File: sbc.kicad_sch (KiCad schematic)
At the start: 2 parts, among them J5 Raspberry_Pi_2_3, J6 Conn_02x07_Odd_Even

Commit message: improve design
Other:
- title: (none) -> Dropbot
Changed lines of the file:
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@@
 	(generator_version "10.0")
 	(paper "A4")
+	(title_block
+		(title "Dropbot")
+	)
 	(junction
 		(at 170.18 92.71)

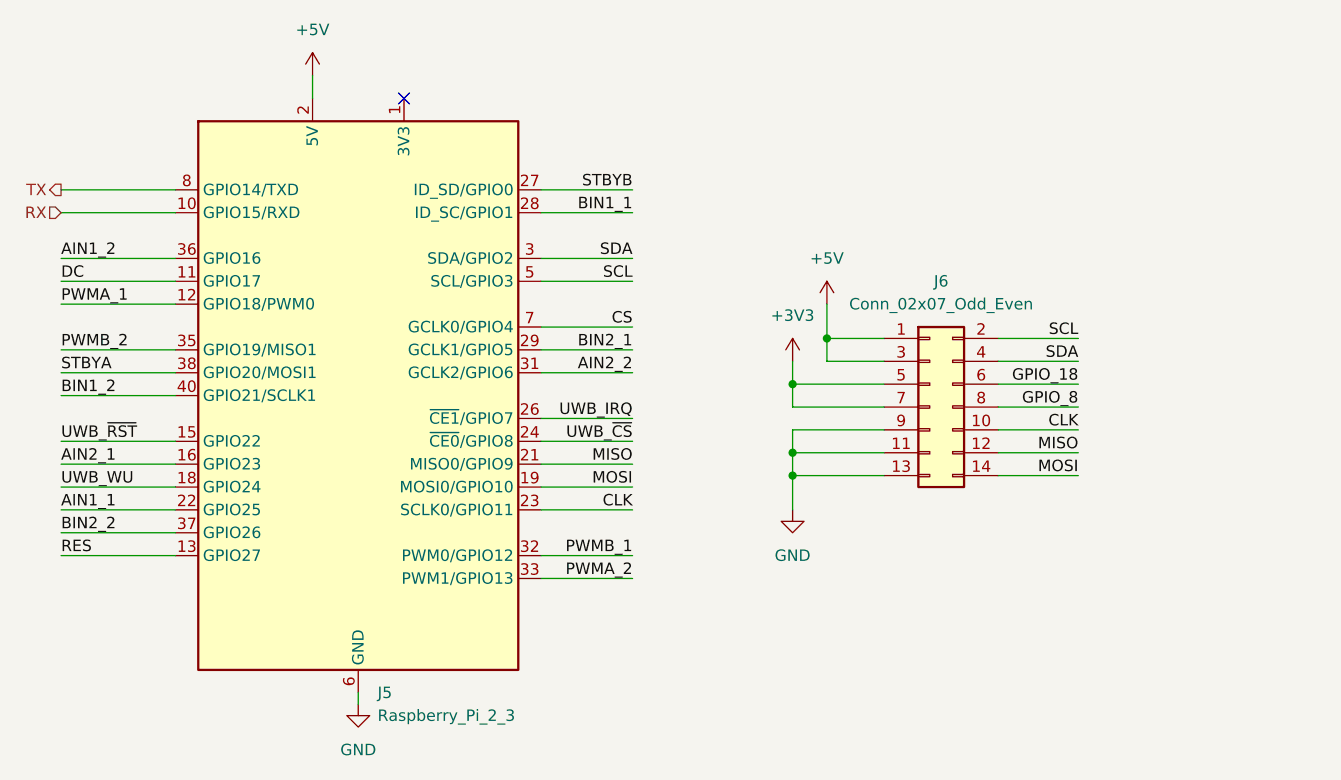
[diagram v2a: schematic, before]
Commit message: consolidated routing
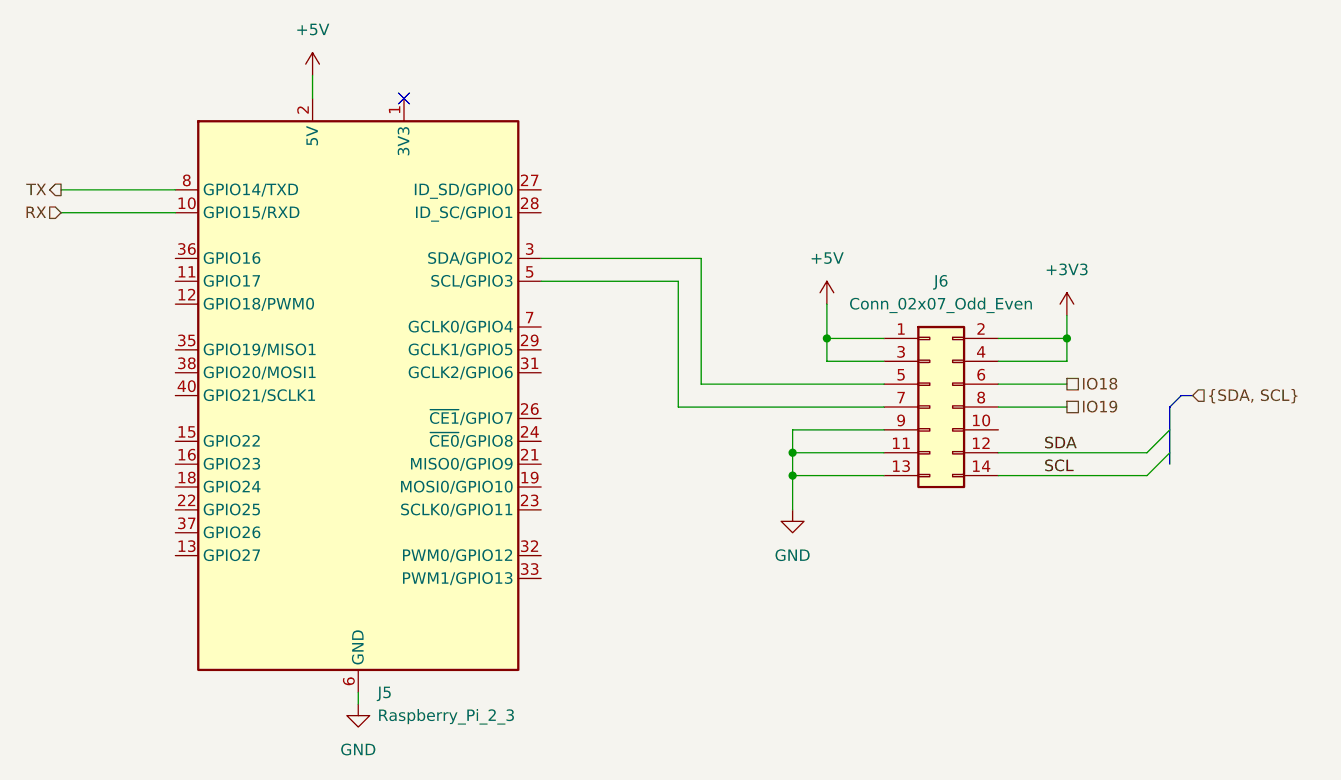
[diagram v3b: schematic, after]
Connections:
- net +3V3: now also J6.2 (Pin_2), J6.4 (Pin_4); no longer J6.5 (Pin_5), J6.7 (Pin_7)
- net SCL: now also J6.14 (Pin_14); no longer J5.5 (SCL/GPIO3), J6.2 (Pin_2)
- net SDA: now also J6.12 (Pin_12); no longer J5.3 (SDA/GPIO2), J6.4 (Pin_4)
- net AIN1_1: no longer names the net of J5.22 (GPIO25)
- net AIN1_2: no longer names the net of J5.36 (GPIO16)
- net AIN2_1: no longer names the net of J5.16 (GPIO23)
- net AIN2_2: no longer names the net of J5.31 (GCLK2/GPIO6)
- net BIN1_1: no longer names the net of J5.28 (ID_SC/GPIO1)
- net BIN1_2: no longer names the net of J5.40 (GPIO21/SCLK1)
- net BIN2_1: no longer names the net of J5.29 (GCLK1/GPIO5)
- net BIN2_2: no longer names the net of J5.37 (GPIO26)
- net CLK: no longer names the net of J6.10 (Pin_10)
- net CLK: no longer J5.23 (SCLK0/GPIO11)
- net CS: no longer names the net of J5.7 (GCLK0/GPIO4)
- net DC: no longer names the net of J5.11 (GPIO17)
- net GPIO_18 renamed IO18
- net GPIO_8 renamed IO19
- net MISO: no longer names the net of J5.21 (MISO0/GPIO9)
- net MISO: no longer J6.12 (Pin_12)
- net MOSI: no longer names the net of J5.19 (MOSI0/GPIO10)
- net MOSI: no longer J6.14 (Pin_14)
- net PWMA_1: no longer names the net of J5.12 (GPIO18/PWM0)
- net PWMA_2: no longer names the net of J5.33 (PWM1/GPIO13)
- net PWMB_1: no longer names the net of J5.32 (PWM0/GPIO12)
- net PWMB_2: no longer names the net of J5.35 (GPIO19/MISO1)
- net RES: no longer names the net of J5.13 (GPIO27)
- net STBYA: no longer names the net of J5.38 (GPIO20/MOSI1)
- net STBYB: no longer names the net of J5.27 (ID_SD/GPIO0)
- net UWB_IRQ: no longer names the net of J5.26 (~{CE1}/GPIO7)
- net UWB_WU: no longer names the net of J5.18 (GPIO24)
- net UWB_~{CS}: no longer names the net of J5.24 (~{CE0}/GPIO8)
- net UWB_~{RST}: no longer names the net of J5.15 (GPIO22)
- new net: J5.3 (SDA/GPIO2), J6.5 (Pin_5)
- new net: J5.5 (SCL/GPIO3), J6.7 (Pin_7)

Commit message: complete routing and validated ERC/DRC
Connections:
- no-connect marks 1 -> 26
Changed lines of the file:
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@@
+	)
+	(no_connect
+		(at 101.6 93.98)
+	)
+	(no_connect
+		(at 142.24 111.76)
 	)
 	(no_connect
 		(at 127 60.96)
 	)
+	(no_connect
+		(at 101.6 101.6)
+	)
+	(no_connect
+		(at 142.24 104.14)
+	)
+	(no_connect
+		(at 101.6 111.76)
+	)
+	(no_connect
+		(at 142.24 114.3)
+	)
+	(no_connect
+		(at 142.24 96.52)
+	)
+	(no_connect
+		(at 101.6 83.82)
+	)
+	(no_connect
+		(at 101.6 78.74)
+	)
+	(no_connect
+		(at 142.24 101.6)
+	)
+	(no_connect
+		(at 101.6 88.9)
+	)
+	(no_connect
+		(at 142.24 99.06)
+	)
+	(no_connect
+		(at 101.6 99.06)
+	)
+	(no_connect
+		(at 193.04 97.79)
+	)
+	(no_connect
+		(at 142.24 91.44)
+	)
+	(no_connect
+		(at 142.24 88.9)
+	)
+	(no_connect
+		(at 142.24 71.12)
+	)
+	(no_connect
+		(at 142.24 86.36)
+	)
+	(no_connect
+		(at 142.24 106.68)
+	)
+	(no_connect
+		(at 101.6 109.22)
+	)
+	(no_connect
+		(at 101.6 81.28)
+	)
+	(no_connect
+		(at 101.6 106.68)
+	)
+	(no_connect
+		(at 142.24 73.66)
+	)
+	(no_connect
+		(at 101.6 104.14)
+	)
+	(no_connect
+		(at 101.6 91.44)
+	)
 	(bus_entry

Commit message: tentative automatic population
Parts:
- J5: LCSC (none) -> C22436166; MPN (none) -> HC-PM254-8.5H-2x20PS; Manufacturer (none) -> Hong Cheng
- J6: LCSC (none) -> C492424; MPN (none) -> PZ254V-12-14P; Manufacturer (none) -> XFCN
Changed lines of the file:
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@@
 			)
 		)
-		(property "Datasheet" ""
+		(property "Datasheet" "https://datasheet.lcsc.com/datasheet/pdf/7e4d55c01d5aeb1046c811fdaf9e5359.pdf?productCode=C492424"
 			(at 185.42 95.25 0)
 			(hide yes)
@@
 					(size 1.27 1.27)
 				)
+			)
+		)
+		(property "Manufacturer" "XFCN" (at 0 0 0)
+			(effects
+				(font
+					(size 1.27 1.27)
+				)
+				(hide yes)
+			)
+		)
+		(property "MPN" "PZ254V-12-14P" (at 0 0 0)
+			(effects
+				(font
+					(size 1.27 1.27)
+				)
+				(hide yes)
+			)
+		)
+		(property "LCSC" "C492424" (at 0 0 0)
+			(effects
+				(font
+					(size 1.27 1.27)
+				)
+				(hide yes)
 			)
 		)
@@
 			)
 		)
+		(property "Manufacturer" "Hong Cheng" (at 0 0 0)
+			(effects
+				(font
+					(size 1.27 1.27)
+				)
+				(hide yes)
+			)
+		)
+		(property "MPN" "HC-PM254-8.5H-2x20PS" (at 0 0 0)
+			(effects
+				(font
+					(size 1.27 1.27)
+				)
+				(hide yes)
+			)
+		)
+		(property "LCSC" "C22436166" (at 0 0 0)
+			(effects
+				(font
+					(size 1.27 1.27)
+				)
+				(hide yes)
+			)
+		)

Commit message: finalized component selection
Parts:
- J5: value Raspberry_Pi_2_3 -> Raspberry Pi Hat Connector
- J6: value Conn_02x07_Odd_Even -> Expansion Header
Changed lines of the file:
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@@
 			)
 		)
-		(property "Value" "Conn_02x07_Odd_Even"
+		(property "Value" "Expansion Header"
 			(at 186.69 83.82 0)
 			(show_name no)
@@
 			)
 		)
-		(property "Value" "Raspberry_Pi_2_3"
+		(property "Value" "Raspberry Pi Hat Connector"
 			(at 124.0633 129.54 0)
 			(show_name no)

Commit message: add MPS entries
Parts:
- J5: MPN HC-PM254-8.5H-2x20PS -> 953240-2000-AR-PR; Manufacturer Hong Cheng -> 3M
- J6: MPN PZ254V-12-14P -> 61201421621; Manufacturer XFCN -> Wurth Elektronik
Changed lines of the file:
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@@
 			)
 		)
-		(property "Manufacturer" "XFCN"
-			(at 0 0 0)
-			(hide yes)
-			(show_name no)
-			(do_not_autoplace no)
-			(effects
-				(font
-					(size 1.27 1.27)
-				)
-			)
-		)
-		(property "MPN" "PZ254V-12-14P"
+		(property "Manufacturer" "Wurth Elektronik"
+			(at 0 0 0)
+			(hide yes)
+			(show_name no)
+			(do_not_autoplace no)
+			(effects
+				(font
+					(size 1.27 1.27)
+				)
+			)
+		)
+		(property "MPN" "61201421621"
 			(at 0 0 0)
 			(hide yes)
@@
 			)
 		)
-		(property "Manufacturer" "Hong Cheng"
-			(at 0 0 0)
-			(hide yes)
-			(show_name no)
-			(do_not_autoplace no)
-			(effects
-				(font
-					(size 1.27 1.27)
-				)
-			)
-		)
-		(property "MPN" "HC-PM254-8.5H-2x20PS"
-			(at 0 0 0)
-			(hide yes)
+		(property "Manufacturer" "3M"
+			(at 0 0 0)
+			(hide yes)
+			(show_name no)
+			(do_not_autoplace no)
+			(effects
+				(font
+					(size 1.27 1.27)
+				)
+			)
+		)
+		(property "MPN" "953240-2000-AR-PR"
+			(at 0 0 0)
+			(hide yes)
